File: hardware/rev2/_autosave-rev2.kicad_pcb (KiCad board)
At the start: 2 copper layers, 24 parts, among them J1 Conn_01x09_Female, J2 RFM9X_header, J3 Conn_02x03_Odd_Even, U2 MPL3115A2, U3 Teensy3.6, U5 ADXL345BCCZ, U7 TPS2113ADRBR

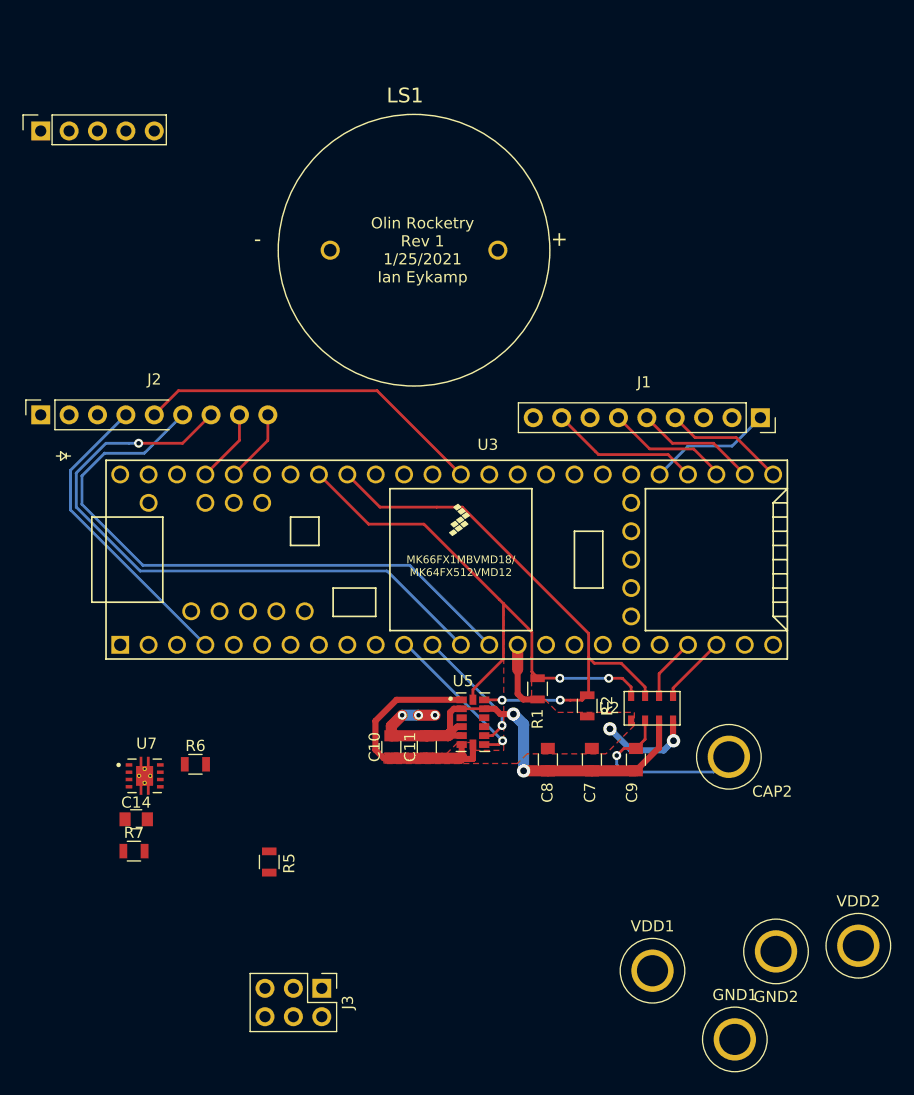
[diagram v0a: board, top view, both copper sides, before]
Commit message: add debugging LEDs (may need to change)
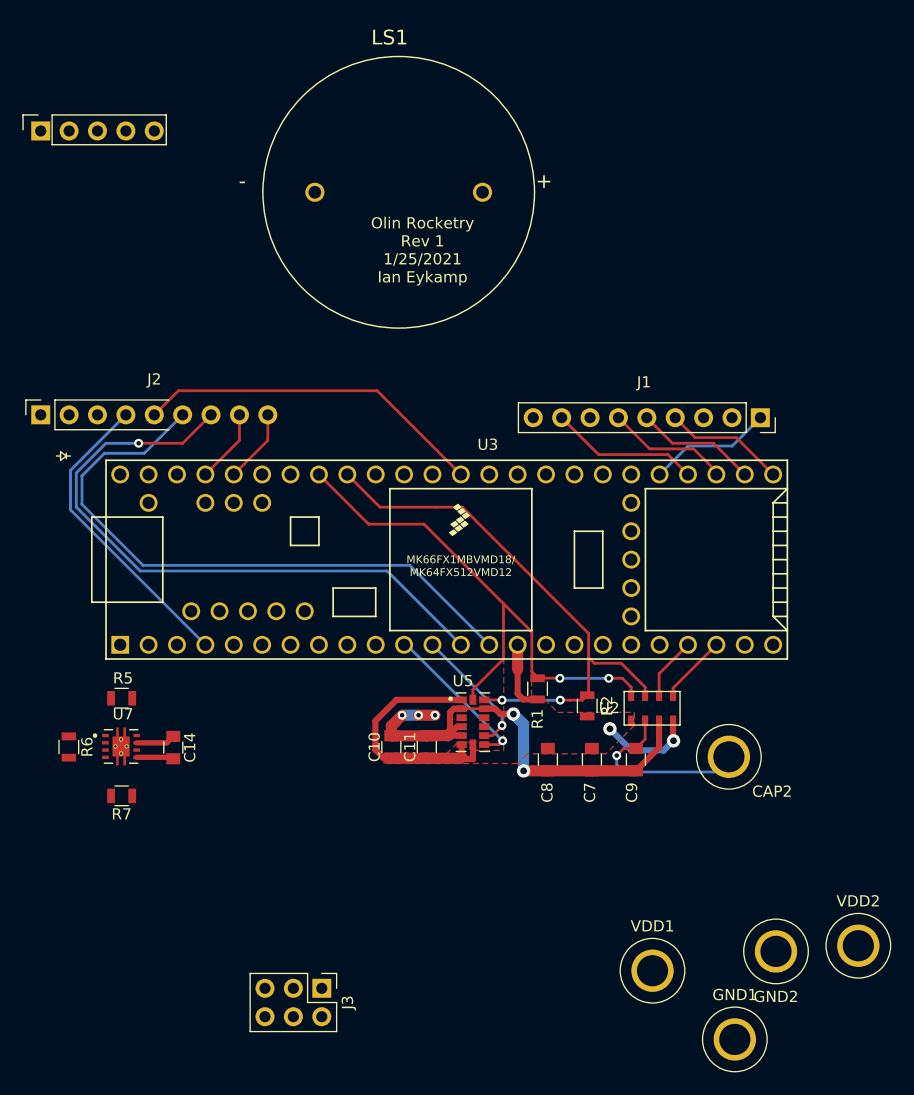
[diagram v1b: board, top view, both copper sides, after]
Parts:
- moved R5 19.7 mm to (115.6, 107.4), turned to 0 degrees
- moved R6 11.4 mm to (110.8, 111.8), turned to 270 degrees
- moved C14 7.22 mm to (120.2, 111.8), turned to 270 degrees
- moved LS1 5.36 mm to (140.4, 62.1)
- moved R7 5.07 mm to (115.6, 116.1), turned to 180 degrees
- moved U7 3.37 mm to (115.5, 111.7)
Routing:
- net BMS_to_Teensy: track 0.00 -> 3.51 mm
- net GND: track 46.1 -> 49.4 mm
